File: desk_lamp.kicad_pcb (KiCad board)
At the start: 2 copper layers, 55 x 37 mm, 31 parts, among them J1 CON-SOCJ-2155, J2 CON-SOCJ-2155, J3 Phoenix_Contact_1989764, Q1 2N7002K, Q2 MCB150N06YB-TP, U1 MCP1799T-3302H_DB, U2 MIC5365-1.2YC5-TR, U3 ECS-TXO-25CSMV-320-AM-TR, U4 ICE40LP384-SG32, U5 W25X10CLSNIG

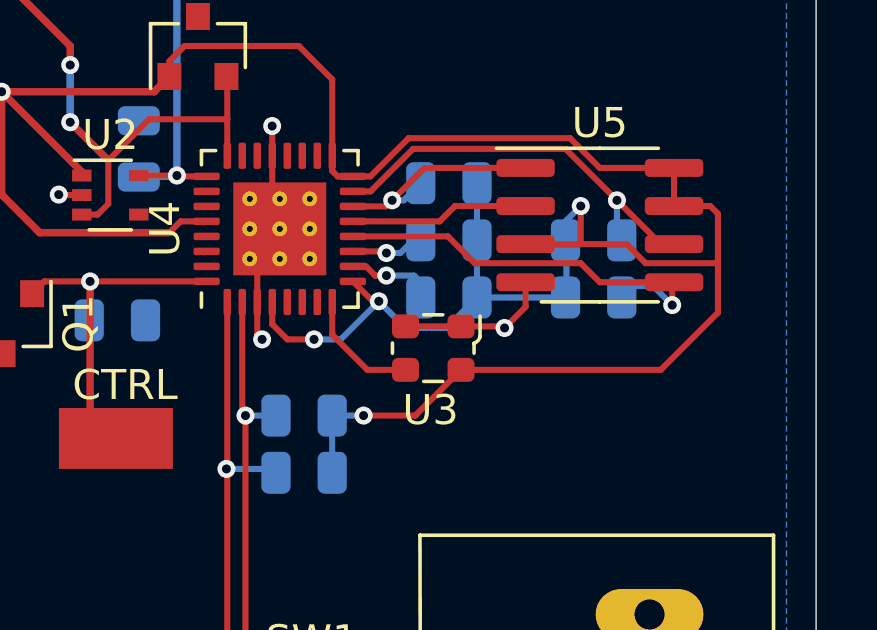
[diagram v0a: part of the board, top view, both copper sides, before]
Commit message: Corrected TCXO and 3V3 LDO
TCXO was replaced with 25MHz that is no longer 0.8Vpp.

LDO did not match footprint. Replaced with compatible model that matched fabbed footprint.

Gerbers updated and could be sent to fab house if desired.
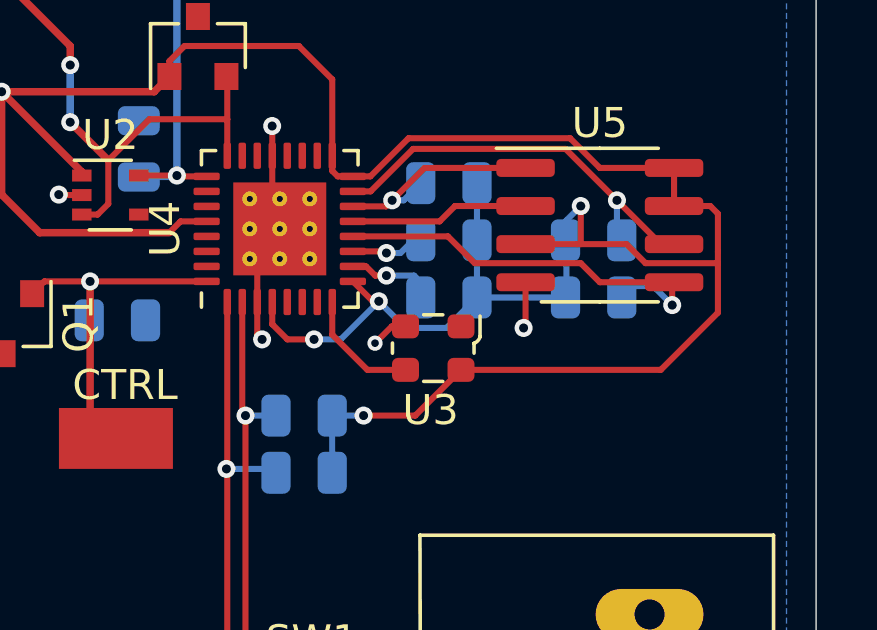
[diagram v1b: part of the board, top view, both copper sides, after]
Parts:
- U1: value MCP1799T-3302H_DB -> MCP1703T-3302E/MB
- U3: value ECS-TXO-25CSMV-320-AM-TR -> ECS-TXO-2520-33-250-AN-TR
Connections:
- U3 pad 1: GND -> Net-(U3-Pad1)
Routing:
- net GND: track 22.9 -> 20.5 mm, vias 6 -> 7

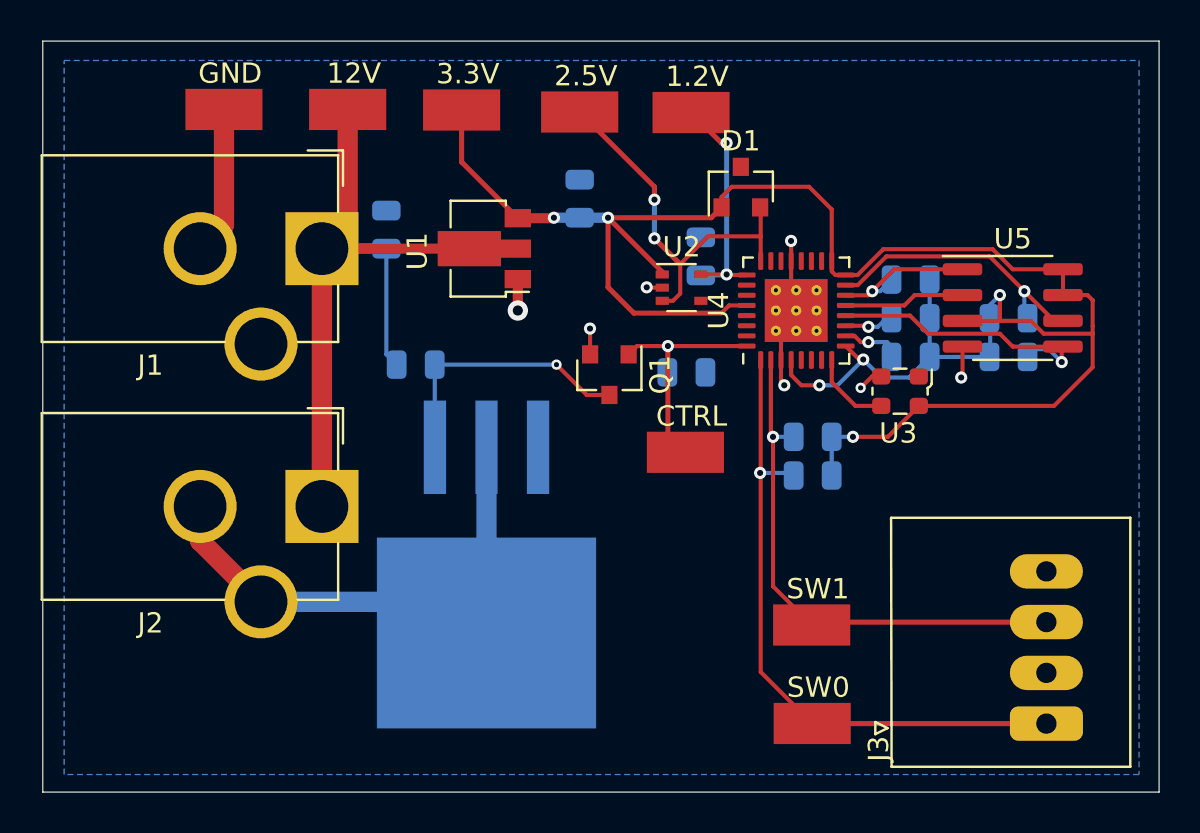
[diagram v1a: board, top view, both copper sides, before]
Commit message: Switched to FPGA module
Switched to FPGA module to make changes easier going forward.
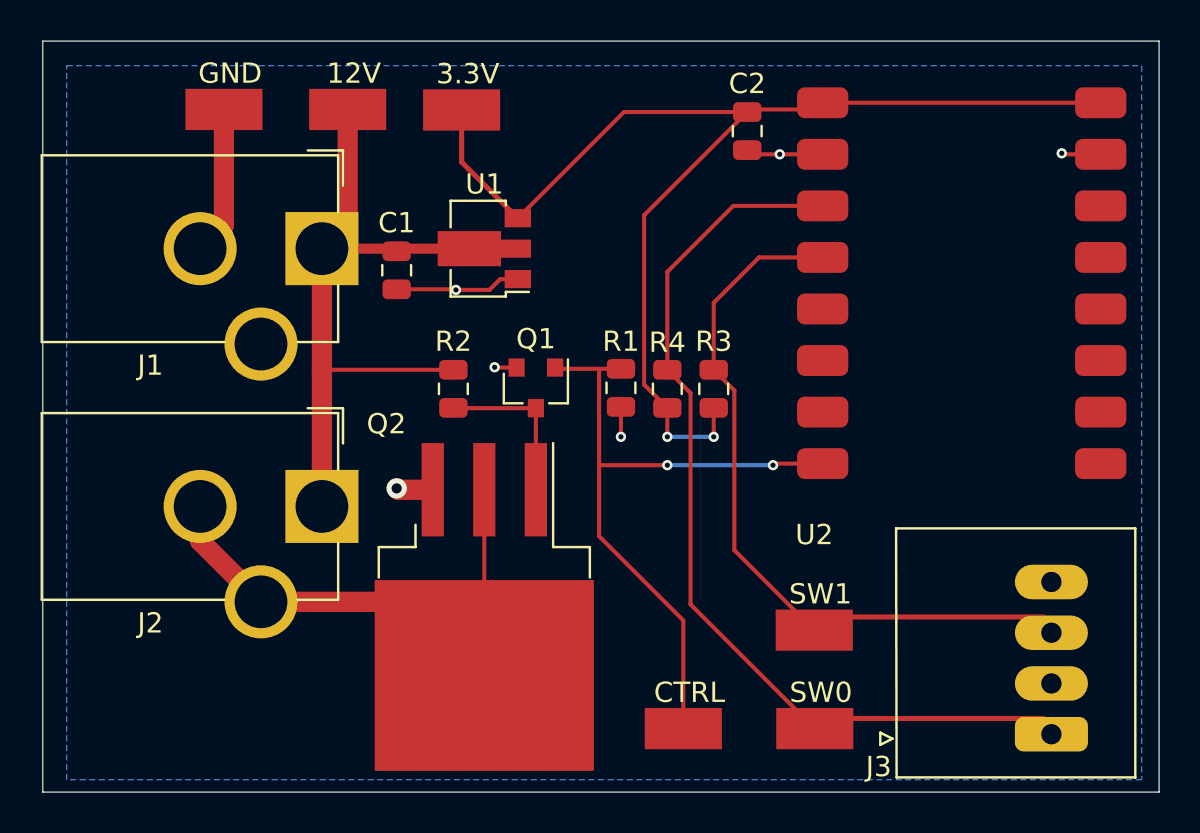
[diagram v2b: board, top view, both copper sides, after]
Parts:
- removed C3: 100n, Capacitor_SMD:C_0805_2012Metric
- removed D1: TBAT54S,LM, nezbyte:SOT-23
- removed R5, R6, R7, R8, R9: 10k, Resistor_SMD:R_0805_2012Metric
- removed TP7: 2.5V, nezbyte:TestPoint_5019
- removed TP8: 1.2V, nezbyte:TestPoint_5019
- removed U3: ECS-TXO-2520-33-250-AN-TR, nezbyte:Oscillator_SMD_ECS_2520MV-xxx-xx-4Pin_2.5x2.0mm
- removed U4: ICE40LP384-SG32, nezbyte:QFN-32-1EP_5x5mm_P0.5mm_EP3.1x3.1mm_ThermalVias
- removed U5: W25X10CLSNIG, nezbyte:SOIC-8_3.9x4.9mm_P1.27mm
- C1, C2, Q2, R1, R2, R3, R4: moved to F.Cu
- U2: value MIC5365-1.2YC5-TR -> ICE30LP384_QFN32_MODULE; footprint nezbyte:SOT-353_SC-70-5 -> nezbyte:ICE30LP384_QFN32_MODULE
- moved U2 13.8 mm to (95.2, 31.8)
- moved TP5 13.6 mm to (81.5, 53.8)
- moved C2 8.90 mm to (84.7, 24.4), turned to 270 degrees
- moved R4 8.34 mm to (80.8, 37.1), turned to 90 degrees
- moved R3 5.42 mm to (83.1, 37.1), turned to 90 degrees
- moved Q1 3.68 mm to (74.3, 37.1)
- moved R1 3.31 mm to (78.5, 37.1), turned to 270 degrees
- moved R2 2.21 mm to (70.2, 37.1), turned to 270 degrees
- moved Q2 2.10 mm to (71.8, 47.9)
- moved C1 2.07 mm to (67.4, 31.3), turned to 270 degrees
- moved J3 0.58 mm to (92.2, 56.1)
- moved TP4 0.28 mm to (88.0, 49.0)
- moved TP3 0.28 mm to (88.0, 53.8)
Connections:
- U2 pad 3: +2V5 -> I_SW0
- U2 pad 4: Net-(U2-Pad4) -> I_SW1
- U2 pad 5: +1V2 -> (no net)
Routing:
- net +3V3: track 103.2 -> 59.8 mm, vias 6 -> 2
- net Lamp_Control: track 12.9 -> 33.8 mm, vias 1 -> 2
- net +2V5: track 19.2 -> 0.00 mm, vias 2 -> 0
- net MOSI: track 14.0 -> 0.00 mm, vias 1 -> 0
- net SCK: track 14.0 -> 0.00 mm, vias 1 -> 0
- net I_SW0: track 32.2 -> 46.1 mm, vias 1 -> 0
- net +1V2: track 12.5 -> 0.00 mm, vias 2 -> 0
- net I_SW1: track 26.5 -> 36.1 mm, vias 1 -> 0
- net CE0: track 7.48 -> 0.00 mm, vias 1 -> 0
- net MISO: track 5.97 -> 0.00 mm
- net Net-(Q1-Pad3): track 13.3 -> 8.09 mm, vias 1 -> 0
- net CLK: track 4.02 -> 0.00 mm
- net GND: track 20.5 -> 23.7 mm, vias 7 -> 6
- net +12V: track 39.1 -> 36.5 mm
- net CDONE: track 2.56 -> 0.00 mm, vias 1 -> 0
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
